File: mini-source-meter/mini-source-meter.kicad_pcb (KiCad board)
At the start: 2 copper layers, 50.8 x 53.3 mm, 32 parts, among them IC1 ADA4351-2ACPZ-R7, J1 Conn_01x01_Pin, J2 Conn_01x01_Pin, J3 Conn_01x01_Pin, J4 Conn_01x01_Pin, J5 Conn_01x01_Pin, U1 OPA992, U2 OPA992, U3 MCP4725xxx-xCH, U4 MCP4725xxx-xCH

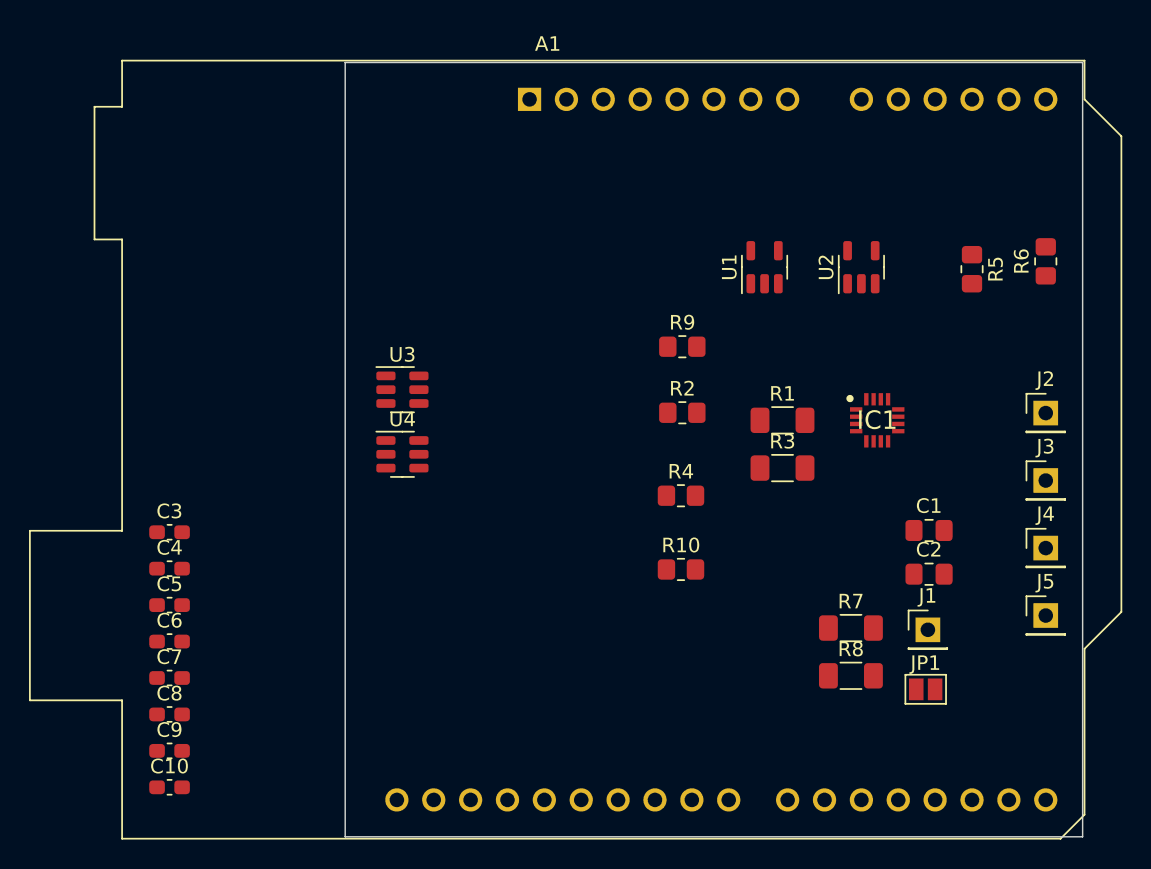
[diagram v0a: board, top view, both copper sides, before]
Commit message: fixed DAC power rails in schmatic
place and routed components on layout
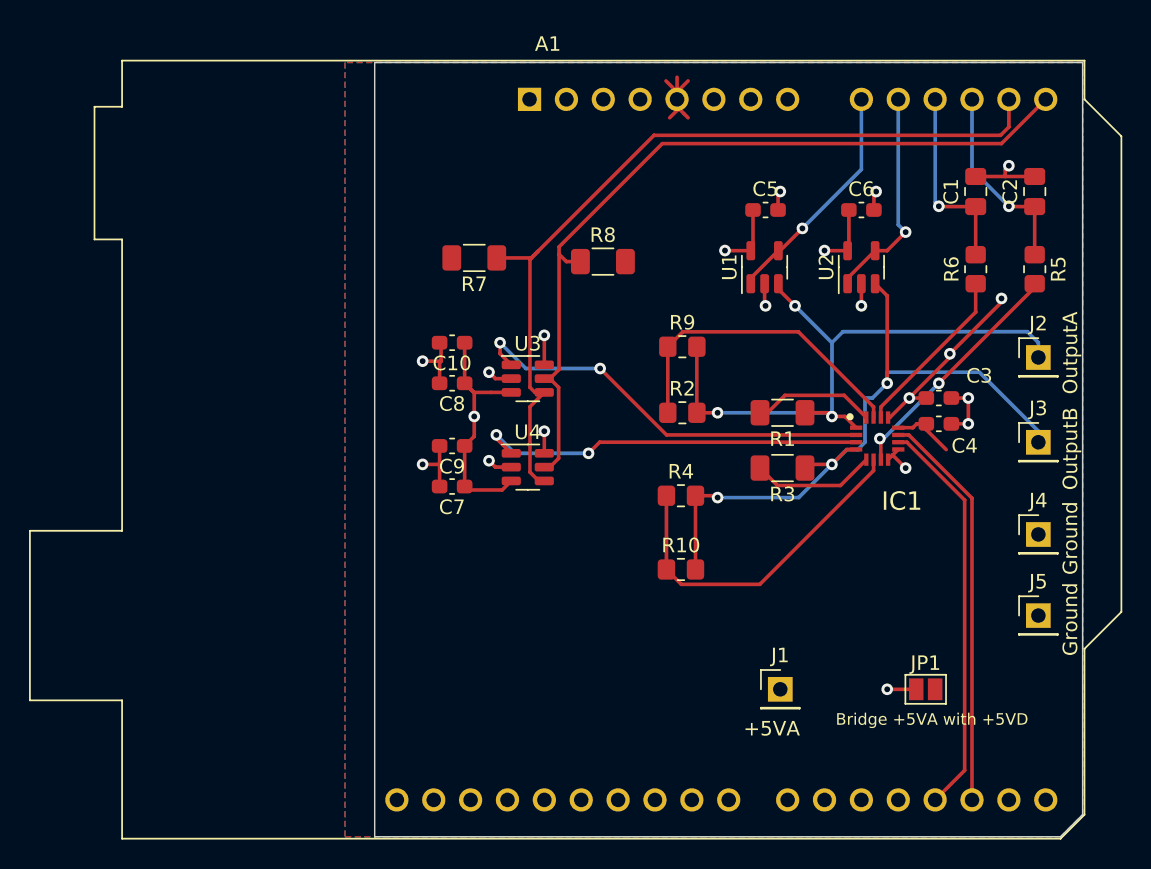
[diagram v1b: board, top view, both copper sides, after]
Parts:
- moved C6 56.2 mm to (94.0, 68.6)
- moved C4 53.9 mm to (99.3, 83.3)
- moved C3 53.8 mm to (99.3, 81.5)
- moved C5 49.3 mm to (87.4, 68.6)
- moved R7 36.4 mm to (67.3, 71.9), turned to 180 degrees
- moved C10 36.3 mm to (65.8, 77.7), turned to 180 degrees
- moved R8 33.3 mm to (76.2, 72.1)
- moved C8 30.0 mm to (65.8, 80.5), turned to 180 degrees
- moved C9 28.6 mm to (65.8, 84.8), turned to 180 degrees
- moved C2 27.3 mm to (105.9, 67.3), turned to 90 degrees
- moved C1 23.6 mm to (101.9, 67.3), turned to 90 degrees
- moved C7 23.5 mm to (65.8, 87.6), turned to 180 degrees
- moved J1 11.0 mm to (88.4, 101.6)
- moved U4 8.68 mm to (71.0, 86.3)
- moved U3 8.67 mm to (71.0, 80.2)
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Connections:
- C2 pad 1: Net-(IC1-OUTB) -> /IoutB
- R1 pad 2: Net-(IC1-SW1_A) -> Net-(IC1-SW0_A)
- R2 pad 1: Net-(IC1-SW0_A) -> Net-(IC1-SW1_A)
- R9 pad 1: Net-(IC1-SW0_A) -> Net-(IC1-SW1_A)
- U3 pad 2: +5VA -> GND
- U3 pad 3: GND -> +5VA
- U4 pad 2: +5VA -> GND
- U4 pad 3: GND -> +5VA
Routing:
- net Net-(U3-SDA): track 0.00 -> 58.8 mm
- net Net-(U3-SCL): track 0.00 -> 56.1 mm
- net /VoutB: track 0.00 -> 48.3 mm, vias 0 -> 3
- net /VoutA: track 0.00 -> 44.5 mm, vias 0 -> 3
- net +5VA: track 0.00 -> 43.0 mm, vias 0 -> 8
- net GND: track 0.00 -> 29.6 mm, vias 0 -> 13
- net /VsetA: track 0.00 -> 29.0 mm, vias 0 -> 2
- net /SW_SEL_B: track 0.00 -> 27.7 mm
- net /SW_SEL_A: track 0.00 -> 27.7 mm
- net /VsetB: track 0.00 -> 27.3 mm, vias 0 -> 2
- net Net-(IC1-SW1_B): track 0.00 -> 23.8 mm
- net Net-(IC1-SW1_A): track 0.00 -> 22.0 mm
- net Net-(IC1-OUTB): track 0.00 -> 16.7 mm, vias 0 -> 2
- net Net-(A1-A0): track 0.00 -> 15.9 mm, vias 0 -> 1
- net Net-(A1-A1): track 0.00 -> 15.1 mm, vias 0 -> 1
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- added copper zone on F.Cu, net +5V
- added copper zone on B.Cu, net +5VA
- added copper zone on In1.Cu, net GND
- added copper zone on In2.Cu, net GND
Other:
- board size 50.8 x 53.3 mm -> 48.8 x 53.3 mm
- copper layers 2 -> 4
- board text added: "+5VA"
- board text added: "Bridge +5VA with +5VD"
- board text added: "Carl Brando"
- board text added: "Ground"
- board text added: "Mini Source Meter"
- board text added: "OutputA"
- board text added: "OutputB"

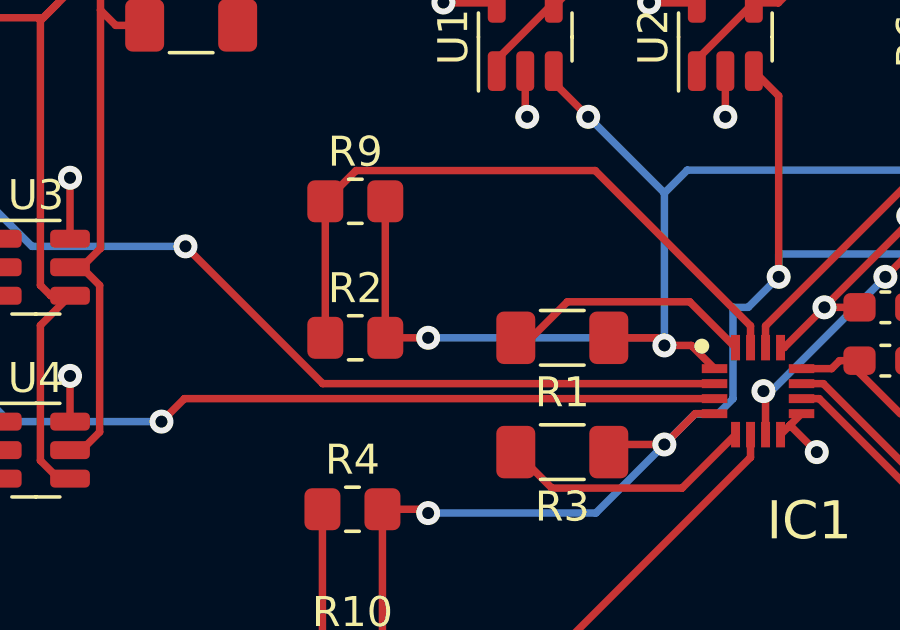
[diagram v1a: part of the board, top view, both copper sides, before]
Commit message: moved a trace
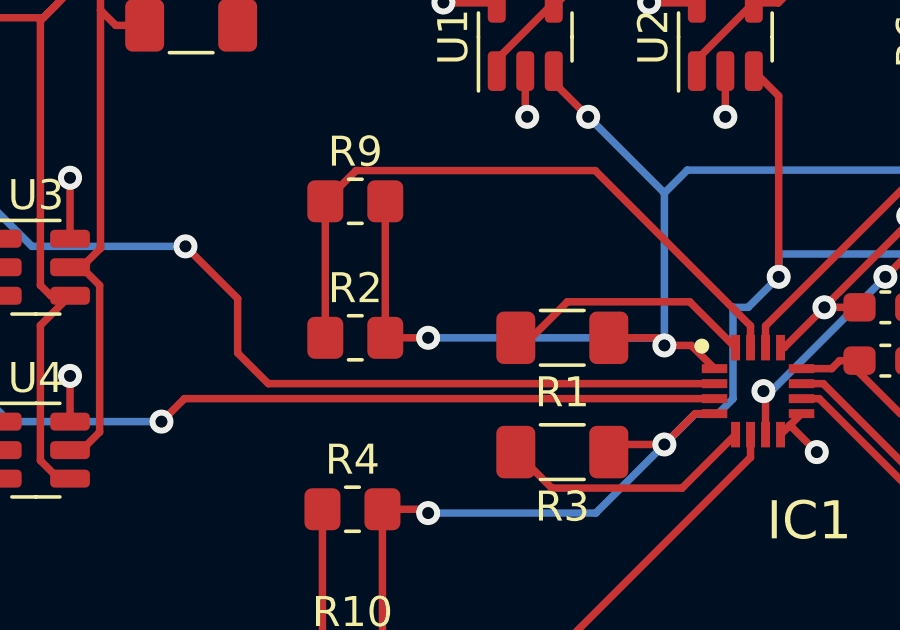
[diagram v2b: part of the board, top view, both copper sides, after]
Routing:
- net /VsetA: track 29.0 -> 30.1 mm
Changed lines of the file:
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@@
   (segment (start 101.092 107.188) (end 99.06 109.22) (width 0.25) (layer "F.Cu") (net 19))
   (segment (start 97.108604 84.578) (end 101.092 88.561396) (width 0.25) (layer "F.Cu") (net 19))
+  (segment (start 77.724 81.242173) (end 75.983827 79.502) (width 0.25) (layer "F.Cu") (net 33))
   (segment (start 69.088 77.724) (end 69.088 78.475) (width 0.25) (layer "F.Cu") (net 33))
+  (segment (start 77.724 83.058) (end 77.724 81.242173) (width 0.25) (layer "F.Cu") (net 33))
+  (segment (start 78.744 84.078) (end 77.724 83.058) (width 0.25) (layer "F.Cu") (net 33))
+  (segment (start 93.62 84.078) (end 78.744 84.078) (width 0.25) (layer "F.Cu") (net 33))
   (segment (start 69.088 78.475) (end 69.861 79.248) (width 0.25) (layer "F.Cu") (net 33))
-  (segment (start 93.62 84.078) (end 80.559827 84.078) (width 0.25) (layer "F.Cu") (net 33))
-  (segment (start 80.559827 84.078) (end 75.983827 79.502) (width 0.25) (layer "F.Cu") (net 33))
   (via (at 69.088 77.724) (size 0.8) (drill 0.4) (layers "F.Cu" "B.Cu") (net 33))
   (via (at 75.983827 79.502) (size 0.8) (drill 0.4) (layers "F.Cu" "B.Cu") (net 33))
